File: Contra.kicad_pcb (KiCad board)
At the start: 2 copper layers, 250.4 x 76.2 mm, 107 parts, among them J1 Conn_01x04, J2 Conn_01x02, SW1 SW_PUSH, SW2 SW_SPDT, U1 ProMicro

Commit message: get all nets connected
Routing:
- net COL11: track 57.0 -> 286.3 mm, vias 0 -> 1
- net COL10: track 57.2 -> 268.2 mm, vias 0 -> 1
- net COL9: track 57.2 -> 251.0 mm, vias 0 -> 1
- net COL8: track 57.2 -> 234.0 mm, vias 0 -> 1
- net COL7: track 57.2 -> 216.9 mm, vias 0 -> 1
- net COL6: track 59.3 -> 202.1 mm, vias 0 -> 1
- net COL5: track 68.8 -> 194.6 mm, vias 0 -> 1
- net COL4: track 57.2 -> 165.7 mm, vias 0 -> 1
- net COL2: track 19.0 -> 104.3 mm, vias 0 -> 2
- net COL3: track 57.2 -> 121.7 mm, vias 0 -> 1
- net Accessory0: track 0.00 -> 33.5 mm
- net COL1: track 57.0 -> 87.0 mm, vias 0 -> 2
- net Accessory1: track 0.00 -> 29.9 mm
- net ROW1: track 251.2 -> 236.0 mm, vias 0 -> 1
- net ROW0: track 246.3 -> 231.3 mm, vias 0 -> 1
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
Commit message: update mounting hole footprints
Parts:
- REF** (x5): value MountingHole_2.2mm_M2_Pad_Via -> MountingHole_2.2mm_M2_Pad; footprint Mounting_Holes:MountingHole_2.2mm_M2_Pad_Via -> MountingHole:MountingHole_2.2mm_M2_Pad
- moved J2 1.22 mm to (36.6, 128.8)
- moved SW2 0.91 mm to (30.5, 125.8)
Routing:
- net VBAT: track 87.8 -> 88.7 mm
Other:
- board text added: "Contra+ PCB by ReillyBex Revision 1.0"
- board text removed: "Contra PCB by ai03 Revision 2.0"

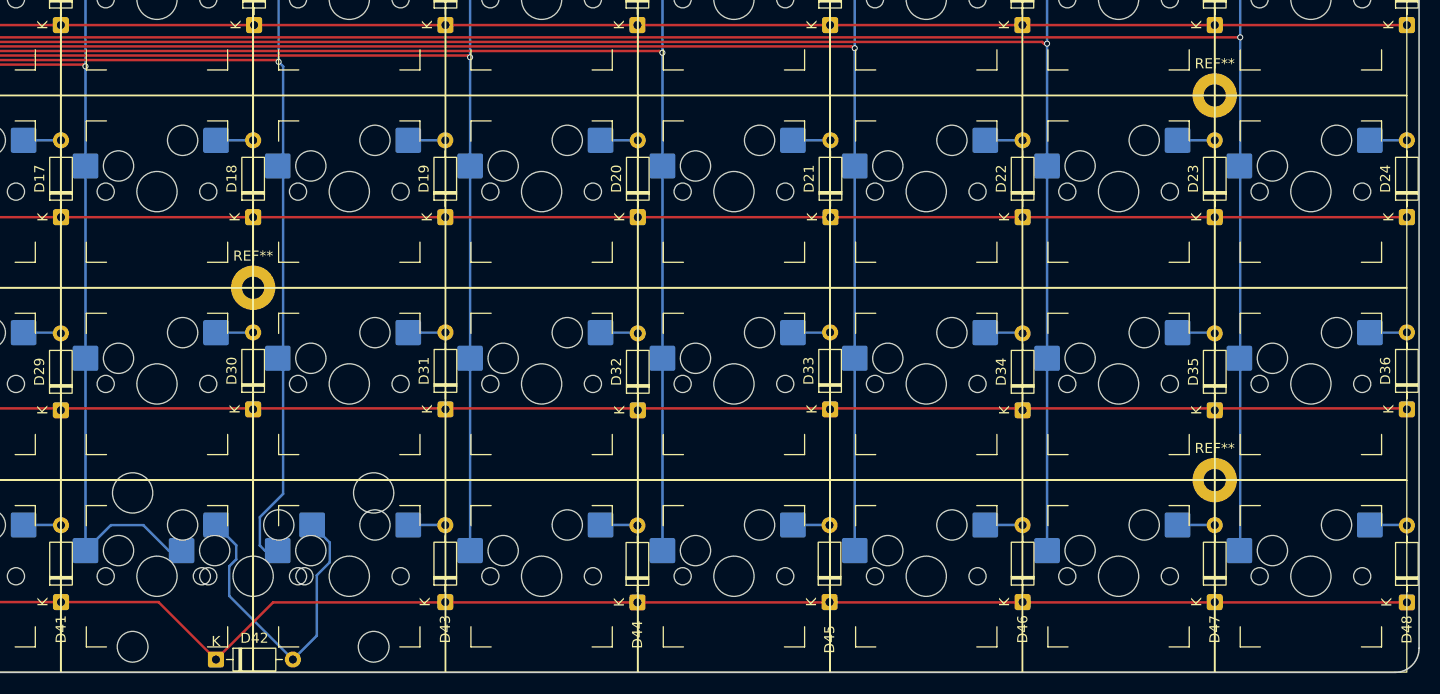
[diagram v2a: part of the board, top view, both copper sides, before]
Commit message: remove 2 1U keys for a single 2U key for space
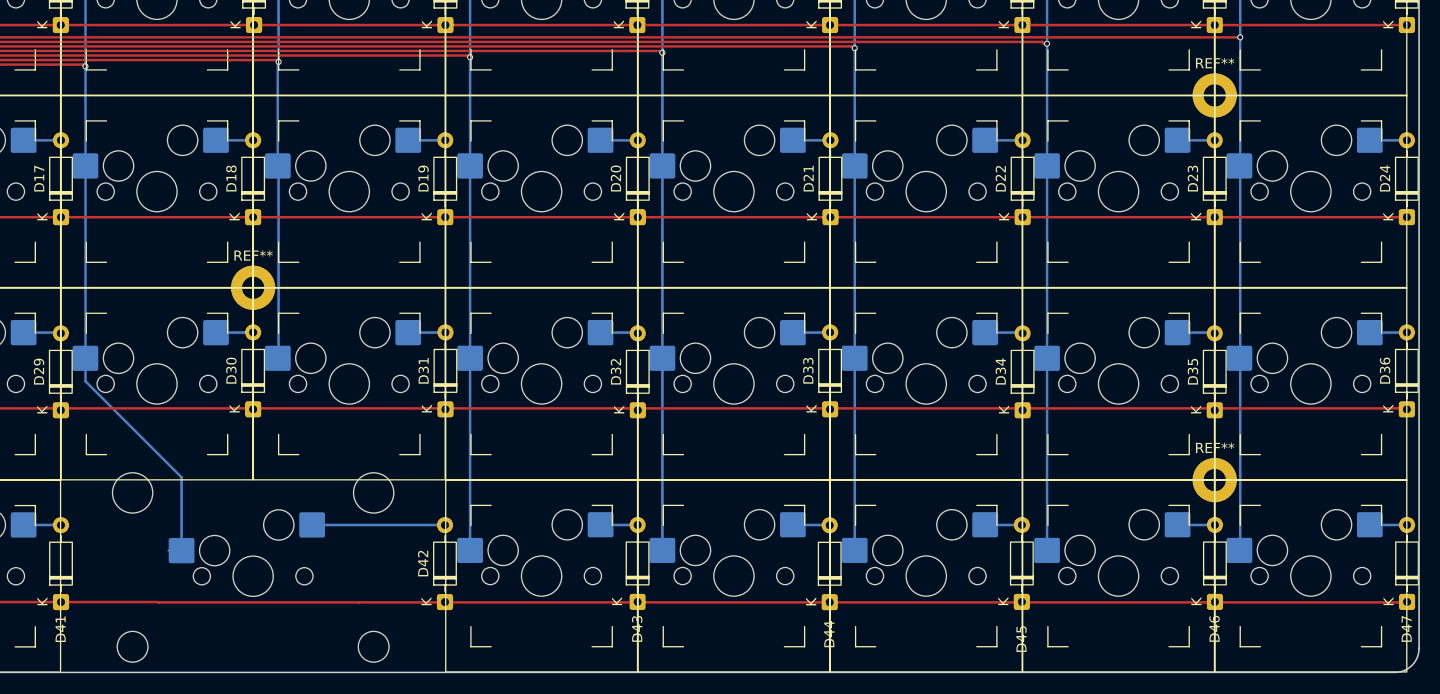
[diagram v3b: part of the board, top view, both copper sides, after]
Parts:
- removed D48: 1N4148, Diode_THT:D_DO-35_SOD27_P7.62mm_Horizontal
- removed MX48: MX-1U, MX_Hotswap:MX-Hotswap-1U
- removed MX49: MX-2U, MX_Hotswap:MX-Hotswap-2U-ReversedStabilizers
- MX42: value MX-1U -> MX-2U; footprint MX_Hotswap:MX-Hotswap-1U -> MX_Hotswap:MX-Hotswap-2U-ReversedStabilizers
- moved D42 23.4 mm to (181.1, 127.3), turned to 90 degrees
- moved D43 19.1 mm to (200.2, 127.3)
- moved D44 19.1 mm to (219.2, 127.3)
- moved D45 19.1 mm to (238.3, 127.3)
- moved D46 19.1 mm to (257.4, 127.3)
- moved D47 19.1 mm to (276.4, 127.3)
- moved MX44 19.1 mm to (209.7, 124.7)
- moved MX45 19.1 mm to (228.8, 124.7)
- moved MX43 19.1 mm to (190.7, 124.7)
- moved MX46 19.1 mm to (247.8, 124.7)
- moved MX47 19.1 mm to (266.9, 124.7)
- moved MX42 9.53 mm to (162.1, 124.7)
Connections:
- MX43 pad 1: COL6 -> COL7
- MX44 pad 1: COL7 -> COL8
- MX45 pad 1: COL8 -> COL9
- MX46 pad 1: COL9 -> COL10
- MX47 pad 1: COL10 -> COL11
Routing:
- net COL6: track 202.4 -> 180.9 mm
- net Net-(D42-A): track 32.6 -> 13.2 mm
- net COL5: track 194.6 -> 188.2 mm
- net ROW3: track 271.8 -> 267.1 mm
- net Net-(D48-A): track 3.61 -> 0.00 mm

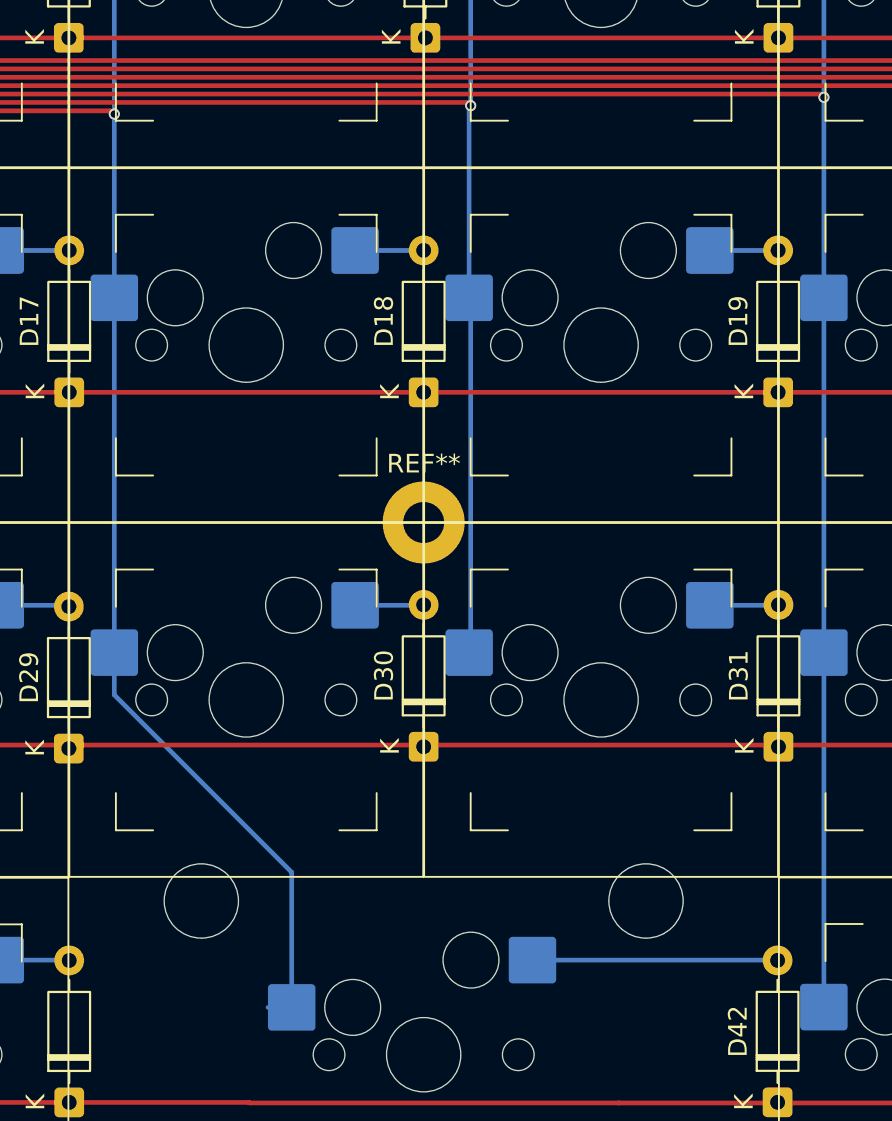
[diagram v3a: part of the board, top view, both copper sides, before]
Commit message: clean up tracks and vias
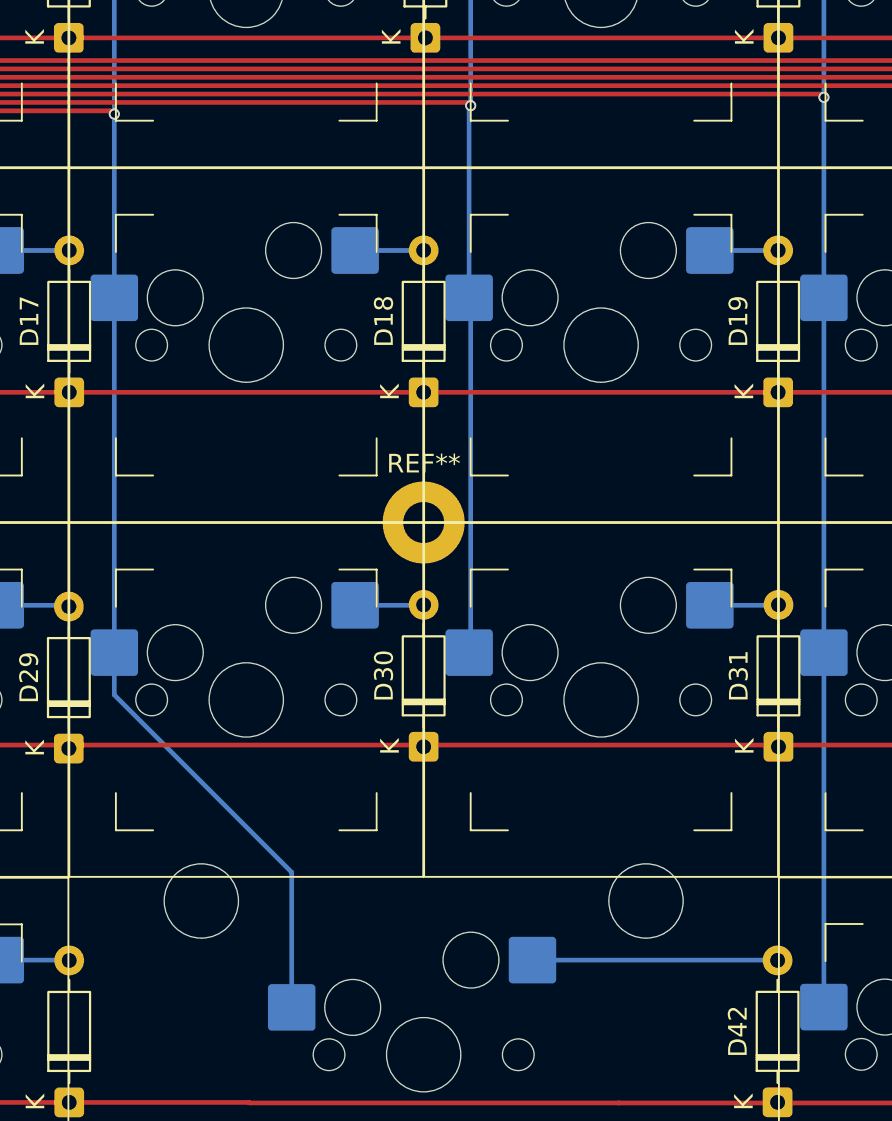
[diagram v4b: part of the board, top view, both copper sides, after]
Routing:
- net COL5: track 188.2 -> 186.9 mm
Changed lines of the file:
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@@
-	)
-	(segment
-		(start 181.11 119.64375)
-		(end 181.125 119.65875)
-		(width 0.25)
-		(layer "B.Cu")
-		(net "Net-(D42-A)")
 	)
 	(segment
@@
 	)
 	(segment
-		(start 153.7625 122.18375)
-		(end 155.0375 122.18375)
-		(width 0.25)
-		(layer "B.Cu")
-		(net "COL5")
-	)
-	(segment
 		(start 145.5125 105.402434)
 		(end 155.0375 114.927434)
-		(width 0.25)
-		(layer "B.Cu")
-		(net "COL5")
-	)
-	(segment
-		(start 145.5125 74.21875)
-		(end 145.5 74.23125)
 		(width 0.25)
 		(layer "B.Cu")
@@
 	)
 	(segment
-		(start 164.5625 84.08375)
-		(end 164.6475 84.16875)
-		(width 0.25)
-		(layer "B.Cu")
-		(net "COL6")
-	)
-	(segment
 		(start 164.5625 73.85375)
 		(end 164.5625 84.08375)
@@
 		(width 0.25)
 		(layer "B.Cu")
-		(net "COL6")
-	)
-	(segment
-		(start 164.6475 103.04875)
-		(end 164.5625 103.13375)
-		(width 0.25)
-		(layer "B.Cu")

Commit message: make PCB 4 layers
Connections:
- SW2 pad 2: VBAT -> Net-(J2-Pin_1)
- SW2 pad 3: Net-(J2-Pin_1) -> VBAT
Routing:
- net COL11: track 286.3 -> 0.00 mm, vias 1 -> 0
- net COL10: track 268.2 -> 0.00 mm, vias 1 -> 0
- net ROW3: track 267.1 -> 0.00 mm, vias 3 -> 0
- net ROW2: track 251.9 -> 0.00 mm, vias 3 -> 0
- net COL9: track 251.0 -> 0.00 mm, vias 1 -> 0
- net ROW1: track 236.0 -> 0.00 mm, vias 1 -> 0
- net COL8: track 234.0 -> 0.00 mm, vias 1 -> 0
- net ROW0: track 231.3 -> 0.00 mm, vias 1 -> 0
- net COL7: track 216.9 -> 0.00 mm, vias 1 -> 0
- net COL5: track 186.9 -> 0.00 mm, vias 1 -> 0
- net COL6: track 180.6 -> 0.00 mm, vias 1 -> 0
- net COL4: track 165.7 -> 0.00 mm, vias 1 -> 0
- net COL3: track 121.7 -> 0.00 mm, vias 1 -> 0
- net COL2: track 104.3 -> 0.00 mm, vias 2 -> 0
- net VBAT: track 88.7 -> 0.00 mm
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- added copper zone on In2.Cu, net GND
- added copper zone on In1.Cu, net VBAT
- removed copper zone on F.Cu, net GND
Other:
- copper layers 2 -> 4

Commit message: update to match Corne PCB settings
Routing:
- net Net-(J2-Pin_1): track 7.07 -> 0.00 mm
- removed copper zone on In2.Cu, net GND
- removed copper zone on In1.Cu, net VBAT
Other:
- copper layers 4 -> 2
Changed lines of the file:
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@@
 	(layers
 		(0 "F.Cu" signal)
-		(4 "In1.Cu" signal)
-		(6 "In2.Cu" signal)
 		(2 "B.Cu" signal)
 		(9 "F.Adhes" user "F.Adhesive")
@@
 			)
 			(layer "dielectric 1"
-				(type "prepreg")
-				(thickness 0.1)
-				(material "FR4")
-				(epsilon_r 4.5)
-				(loss_tangent 0.02)
-			)
-			(layer "In1.Cu"
-				(type "copper")
-				(thickness 0.035)
-			)
-			(layer "dielectric 2"
 				(type "core")
-				(thickness 1.24)
-				(material "FR4")
-				(epsilon_r 4.5)
-				(loss_tangent 0.02)
-			)
-			(layer "In2.Cu"
-				(type "copper")
-				(thickness 0.035)
-			)
-			(layer "dielectric 3"
-				(type "prepreg")
-				(thickness 0.1)
+				(thickness 1.51)
 				(material "FR4")
 				(epsilon_r 4.5)
@@
 			)
 		)
-	)
-	(segment
-		(start 36.58625 128.78125)
-		(end 31.58625 123.78125)
-		(width 0.25)
-		(layer "In1.Cu")
-		(net "Net-(J2-Pin_1)")
-	)
-	(zone
-		(net "VBAT")
-		(layer "In1.Cu")
-		(name "Power Plane")
-		(hatch edge 0.5)
-		(priority 1)
-		(connect_pads
-			(clearance 0.381)
-		)
-		(min_thickness 0.25)
-		(fill yes
-			(thermal_gap 0.5)
-			(thermal_bridge_width 0.5)
-			(island_removal_mode 0)
-		)
-		(polygon
-			(pts
-				(xy 27.1875 57.84375) (xy 277.5 57.84375) (xy 277.5 134.25) (xy 27.1875 134.4375)
-			)
-		)
-	)
-	(zone
-		(net "GND")
-		(layer "In2.Cu")
-		(name "Ground Plane")
-		(hatch edge 0.5)
-		(connect_pads
-			(clearance 0.381)
-		)
-		(min_thickness 0.25)
-		(fill yes
-			(thermal_gap 0.5)
-			(thermal_bridge_width 0.5)
-			(island_removal_mode 0)
-		)
-		(polygon
-			(pts
-				(xy 27.058159 57.984537) (xy 277.451306 57.84375) (xy 277.5 134.25) (xy 27.152653 134.430541)
-			)
-		)

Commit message: Place keyswitches in grid
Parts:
- removed REF** (x5): MountingHole_2.2mm_M2_Pad, MountingHole:MountingHole_2.2mm_M2_Pad
- added H1: MountingHole_Pad, MountingHole:MountingHole_2.2mm_M2_Pad, F.Cu at (-82.3, 124.8)
- added H2: MountingHole_Pad, MountingHole:MountingHole_2.2mm_M2_Pad, F.Cu at (-82.3, 130.8)
- added H3: MountingHole_Pad, MountingHole:MountingHole_2.2mm_M2_Pad, F.Cu at (-82.3, 136.8)
- added H4: MountingHole_Pad, MountingHole:MountingHole_2.2mm_M2_Pad, F.Cu at (-82.3, 142.7)
- added H5: MountingHole_Pad, MountingHole:MountingHole_2.2mm_M2_Pad, F.Cu at (-82.3, 148.7)
- added LED1: 4960, kbd:YS-SK6812MINI-E, F.Cu at (319.5, 189.6)
- added LED10: 4960, kbd:YS-SK6812MINI-E, F.Cu at (336.4, 195.6)
- added LED11: 4960, kbd:YS-SK6812MINI-E, F.Cu at (336.4, 201.7)
- added LED12: 4960, kbd:YS-SK6812MINI-E, F.Cu at (336.4, 207.7)
- added LED13: 4960, kbd:YS-SK6812MINI-E, F.Cu at (336.6, 212.8)
- added LED14: 4960, kbd:YS-SK6812MINI-E, F.Cu at (336.6, 217.0)
- added LED15: 4960, kbd:YS-SK6812MINI-E, F.Cu at (336.6, 221.2)
- added LED16: 4960, kbd:YS-SK6812MINI-E, F.Cu at (336.6, 225.4)
- added LED17: 4960, kbd:YS-SK6812MINI-E, F.Cu at (336.6, 229.6)
- added LED18: 4960, kbd:YS-SK6812MINI-E, F.Cu at (336.6, 233.8)
- added LED19: 4960, kbd:YS-SK6812MINI-E, F.Cu at (336.6, 238.0)
- added LED2: 4960, kbd:YS-SK6812MINI-E, F.Cu at (319.5, 195.6)
- added LED20: 4960, kbd:YS-SK6812MINI-E, F.Cu at (336.6, 242.2)
- added LED21: 4960, kbd:YS-SK6812MINI-E, F.Cu at (336.6, 246.4)
- added LED22: 4960, kbd:YS-SK6812MINI-E, F.Cu at (336.6, 250.6)
- added LED23: 4960, kbd:YS-SK6812MINI-E, F.Cu at (345.3, 212.8)
- added LED24: 4960, kbd:YS-SK6812MINI-E, F.Cu at (345.3, 217.0)
- added LED25: 4960, kbd:YS-SK6812MINI-E, F.Cu at (345.3, 221.2)
- added LED26: 4960, kbd:YS-SK6812MINI-E, F.Cu at (345.3, 225.4)
- added LED27: 4960, kbd:YS-SK6812MINI-E, F.Cu at (345.3, 229.6)
- added LED28: 4960, kbd:YS-SK6812MINI-E, F.Cu at (345.3, 233.8)
- added LED29: 4960, kbd:YS-SK6812MINI-E, F.Cu at (345.3, 238.0)
- added LED3: 4960, kbd:YS-SK6812MINI-E, F.Cu at (319.5, 201.7)
- added LED30: 4960, kbd:YS-SK6812MINI-E, F.Cu at (345.3, 242.2)
- added LED31: 4960, kbd:YS-SK6812MINI-E, F.Cu at (345.3, 246.4)
- added LED32: 4960, kbd:YS-SK6812MINI-E, F.Cu at (345.3, 250.6)
- added LED33: 4960, kbd:YS-SK6812MINI-E, F.Cu at (354.1, 212.8)
- added LED34: 4960, kbd:YS-SK6812MINI-E, F.Cu at (354.1, 217.0)
- added LED35: 4960, kbd:YS-SK6812MINI-E, F.Cu at (354.1, 221.2)
- added LED36: 4960, kbd:YS-SK6812MINI-E, F.Cu at (354.1, 225.4)
- added LED37: 4960, kbd:YS-SK6812MINI-E, F.Cu at (354.1, 229.6)
- added LED38: 4960, kbd:YS-SK6812MINI-E, F.Cu at (354.1, 233.8)
- added LED39: 4960, kbd:YS-SK6812MINI-E, F.Cu at (354.1, 238.0)
- added LED4: 4960, kbd:YS-SK6812MINI-E, F.Cu at (319.5, 207.7)
- added LED40: 4960, kbd:YS-SK6812MINI-E, F.Cu at (354.1, 242.2)
- added LED41: 4960, kbd:YS-SK6812MINI-E, F.Cu at (354.1, 246.4)
- added LED42: 4960, kbd:YS-SK6812MINI-E, F.Cu at (354.1, 250.6)
- added LED43: 4960, kbd:YS-SK6812MINI-E, F.Cu at (362.8, 212.8)
- added LED44: 4960, kbd:YS-SK6812MINI-E, F.Cu at (362.8, 217.0)
- added LED45: 4960, kbd:YS-SK6812MINI-E, F.Cu at (362.8, 221.2)
- added LED46: 4960, kbd:YS-SK6812MINI-E, F.Cu at (362.8, 225.4)
- added LED47: 4960, kbd:YS-SK6812MINI-E, F.Cu at (362.8, 229.6)
- added LED48: 4960, kbd:YS-SK6812MINI-E, F.Cu at (362.8, 233.8)
- added LED5: 4960, kbd:YS-SK6812MINI-E, F.Cu at (328.0, 189.6)
- added LED6: 4960, kbd:YS-SK6812MINI-E, F.Cu at (328.0, 195.6)
- added LED7: 4960, kbd:YS-SK6812MINI-E, F.Cu at (328.0, 201.7)
- added LED8: 4960, kbd:YS-SK6812MINI-E, F.Cu at (328.0, 207.7)
- added LED9: 4960, kbd:YS-SK6812MINI-E, F.Cu at (336.4, 189.6)
- J1: value Conn_01x04 -> Conn_01x03; footprint Connector_PinHeader_2.54mm:PinHeader_1x04_P2.54mm_Horizontal -> Connector_PinHeader_2.54mm:PinHeader_1x03_P2.54mm_Horizontal
- MX1, MX10, MX11, MX12, MX13, MX14, MX15, MX16, MX17, MX18, MX19, MX2, MX20, MX21, MX22, MX23, MX24, MX25, MX26, MX27, MX28, MX29, MX3, MX30, MX31, MX32, MX33, MX34, MX35, MX36, MX37, MX38, MX39, MX4, MX40, MX41, MX42, MX43, MX44, MX45, MX46, MX47, MX5, MX6, MX7, MX8, MX9: moved to F.Cu
- moved D37 415.7 mm to (469.7, 24.8), turned to 0 degrees
- moved D25 400.8 mm to (459.0, 24.8), turned to 0 degrees
- moved D38 396.4 mm to (469.7, 28.4), turned to 0 degrees
- moved D13 386.7 mm to (448.2, 24.8), turned to 0 degrees
- moved D26 381.5 mm to (459.0, 28.4), turned to 0 degrees
- moved D39 377.0 mm to (469.7, 31.9), turned to 0 degrees
- moved D1 373.3 mm to (437.4, 24.8), turned to 0 degrees
- moved D14 367.4 mm to (448.2, 28.4), turned to 0 degrees
- moved D27 362.1 mm to (459.0, 31.9), turned to 0 degrees
- moved D40 357.7 mm to (469.7, 35.5), turned to 0 degrees
- moved D2 353.9 mm to (437.4, 28.4), turned to 0 degrees
- moved D15 348.0 mm to (448.2, 31.9), turned to 0 degrees
- moved D28 342.8 mm to (459.0, 35.5), turned to 0 degrees
- moved D41 338.4 mm to (469.7, 39.0), turned to 0 degrees
- moved D3 334.7 mm to (437.4, 31.9), turned to 0 degrees
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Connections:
- J1 pad 2: Accessory0 -> Accessory1
- J1 pad 3: Accessory1 -> VBAT
- U1 pad 1: Accessory0 -> NeopixelDin
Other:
- board size 250.4 x 76.2 mm -> 3.6 x 3.1 mm
- board text removed: "Contra+ PCB by ReillyBex Revision 1.0"

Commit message: Place Diodes
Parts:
- MX1, MX10, MX11, MX12, MX13, MX14, MX15, MX16, MX17, MX18, MX19, MX2, MX20, MX21, MX22, MX23, MX24, MX25, MX26, MX27, MX28, MX29, MX3, MX30, MX31, MX32, MX33, MX34, MX35, MX36, MX37, MX38, MX39, MX4, MX40, MX41, MX42, MX43, MX44, MX45, MX46, MX47, MX5, MX6, MX7, MX8, MX9: moved to B.Cu
- moved D37 427.2 mm to (52.4, 116.2), turned to 90 degrees
- moved D25 413.0 mm to (52.4, 97.2), turned to 90 degrees
- moved D38 407.9 mm to (71.4, 116.2), turned to 90 degrees
- moved D13 399.4 mm to (52.4, 78.1), turned to 90 degrees
- moved D26 393.6 mm to (71.4, 97.2), turned to 90 degrees
- moved D39 388.5 mm to (90.5, 116.2), turned to 90 degrees
- moved D1 386.6 mm to (52.4, 59.1), turned to 90 degrees
- moved D14 380.0 mm to (71.4, 78.1), turned to 90 degrees
- moved D27 374.2 mm to (90.5, 97.2), turned to 90 degrees
- moved D40 369.1 mm to (109.5, 116.2), turned to 90 degrees
- moved D2 367.3 mm to (71.4, 59.1), turned to 90 degrees
- moved D15 360.7 mm to (90.5, 78.1), turned to 90 degrees
- moved D28 354.8 mm to (109.5, 97.2), turned to 90 degrees
- moved D41 349.8 mm to (128.6, 116.2), turned to 90 degrees
- moved D3 348.0 mm to (90.5, 59.1), turned to 90 degrees
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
